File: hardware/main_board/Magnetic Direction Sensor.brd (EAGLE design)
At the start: 49.9 x 49.6 mm, 8 parts, among them J1 5520425-3, J2 5520425-3

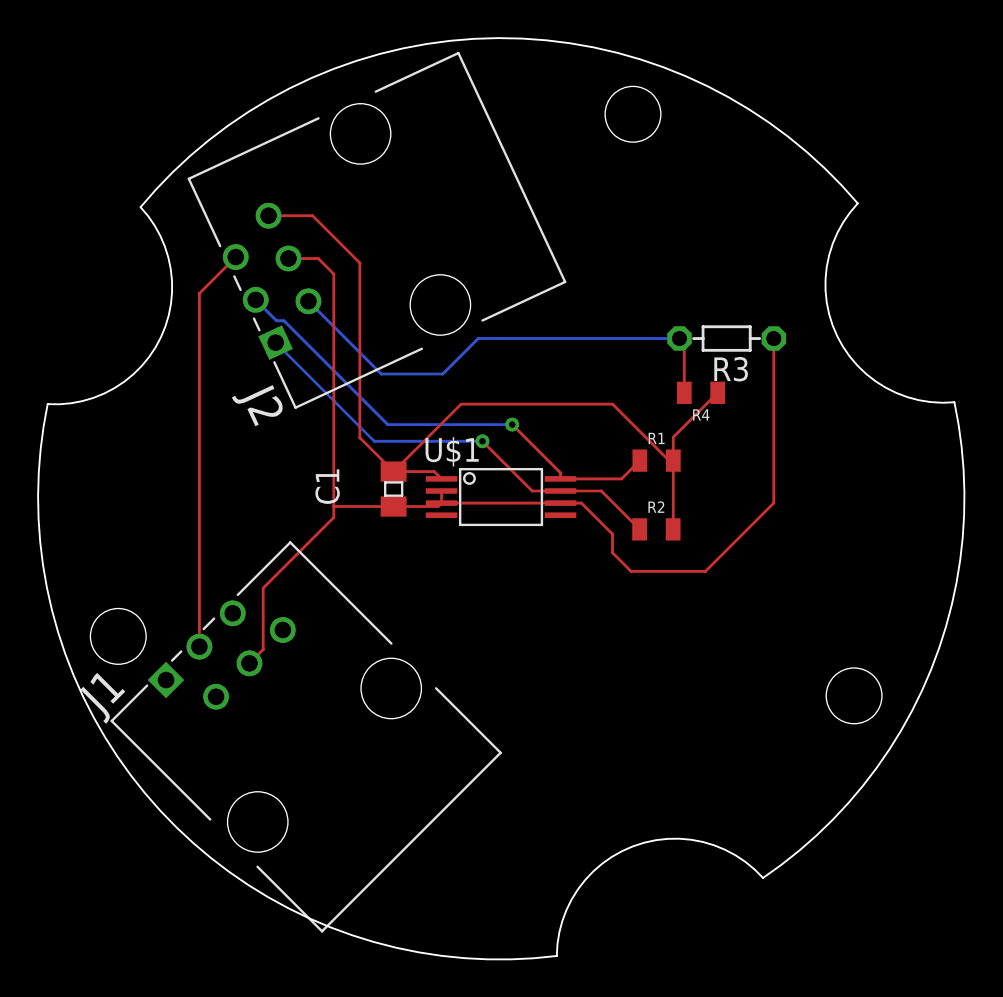
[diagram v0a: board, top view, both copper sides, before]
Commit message: Hardware work. Added elevation to station meta data
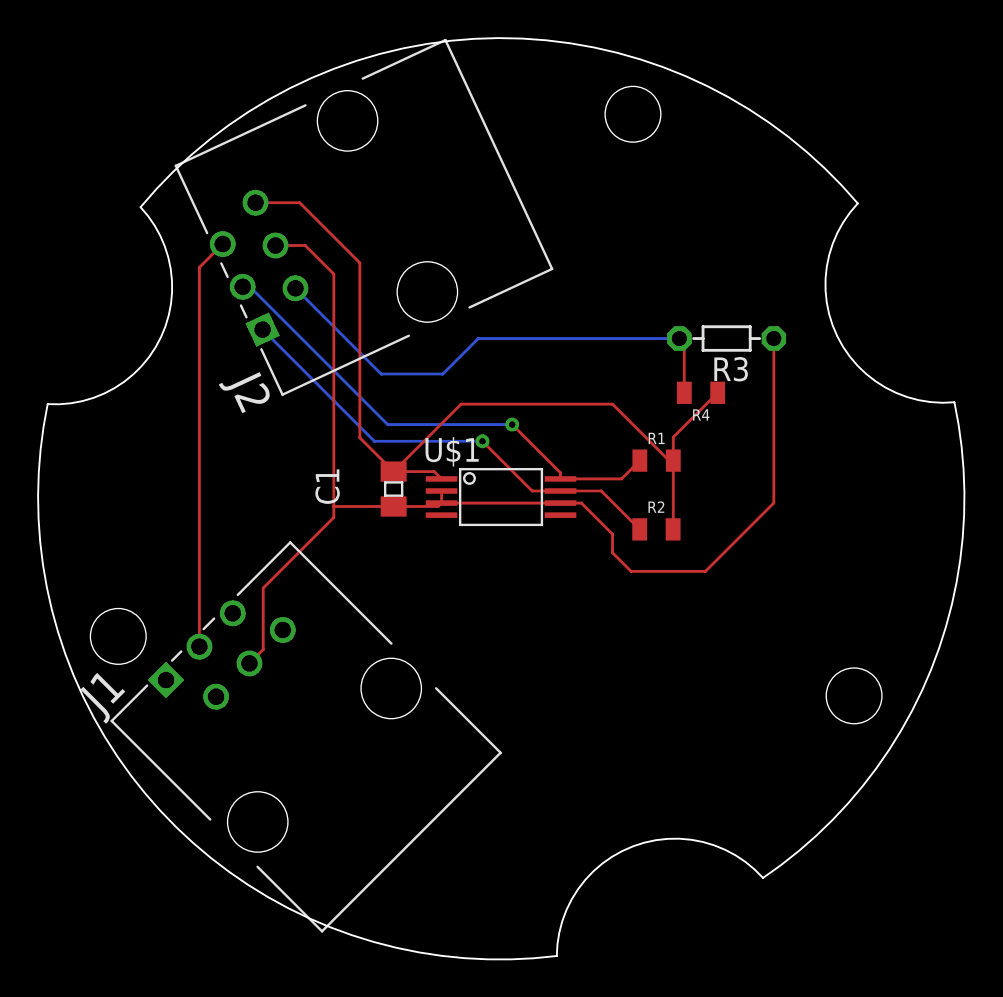
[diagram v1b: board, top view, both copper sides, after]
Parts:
- moved J2 0.99 mm to (12.2, 34.0)
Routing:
- net TS2: track 25.4 -> 26.4 mm
- net SCL: track 25.3 -> 26.3 mm
- net VCC: track 46.8 -> 47.8 mm
- net GND: track 62.5 -> 63.5 mm
- net SDA: track 23.8 -> 24.7 mm
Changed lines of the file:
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@@
 <attribute name="VALUE" x="17.09809375" y="-0.045665625" size="1.77965" layer="27" rot="R45"/>
 </element>
-<element name="J2" library="main_board" package="TE_5520425-3" value="5520425-3" x="12.87" y="33.31" smashed="yes" rot="R115">
-<attribute name="CENTERLINE_PITCH" value="1.02 mm[.04 in]" x="40.655575" y="72.89113125" size="1.778" layer="27" rot="R115" display="off"/>
-<attribute name="COMMENT" value="5520425-3" x="40.655575" y="72.89113125" size="1.778" layer="27" rot="R115" display="off"/>
-<attribute name="DESCRIPTION" value=" Conn RJ-25 F 6 POS 2.54mm Solder ST Thru-Hole 6 Terminal 1 Port Cat 3 Box/Package/Tray " x="40.655575" y="72.89113125" size="1.778" layer="27" rot="R115" display="off"/>
-<attribute name="DIGI-KEY_PART_NUMBER" value="A31415-ND" x="40.655575" y="72.89113125" size="1.778" layer="27" rot="R115" display="off"/>
-<attribute name="DIGI-KEY_PURCHASE_URL" value="https://www.digikey.com/product-detail/en/te-connectivity-amp-connectors/5520425-3/A31415-ND/769559?utm_source=snapeda&amp;utm_medium=aggregator&amp;utm_campaign=symbol" x="40.655575" y="72.89113125" size="1.778" layer="27" rot="R115" display="off"/>
-<attribute name="EU_ROHS_COMPLIANCE" value="Compliant" x="40.655575" y="72.89113125" size="1.778" layer="27" rot="R115" display="off"/>
-<attribute name="MF" value="TE Connectivity" x="40.655575" y="72.89113125" size="1.778" layer="27" rot="R115" display="off"/>
-<attribute name="MP" value="5520425-3" x="40.655575" y="72.89113125" size="1.778" layer="27" rot="R115" display="off"/>
-<attribute name="NAME" x="13.48356875" y="29.363684375" size="1.78073125" layer="25" rot="R115"/>
-<attribute name="NUMBER_OF_POSITIONS" value="6" x="40.655575" y="72.89113125" size="1.778" layer="27" rot="R115" display="off"/>
-<attribute name="PACKAGE" value="None" x="40.655575" y="72.89113125" size="1.778" layer="27" rot="R115" display="off"/>
-<attribute name="TE_PURCHASE_URL" value="https://www.te.com/usa-en/product-5520425-3.html?te_bu=Cor&amp;te_type=disp&amp;te_campaign=seda_glo_cor-seda-global-disp-prtnr-fy19-seda-model-bom-cta_sma-317_1&amp;elqCampaignId=32493" x="40.655575" y="72.89113125" size="1.778" layer="27" rot="R115" display="off"/>
-<attribute name="VALUE" x="30.6132625" y="37.630059375" size="1.77965" layer="27" rot="R115"/>
+<element name="J2" library="main_board" package="TE_5520425-3" value="5520425-3" x="12.17" y="34.01" smashed="yes" rot="R115">
+<attribute name="CENTERLINE_PITCH" value="1.02 mm[.04 in]" x="39.955575" y="73.59113125" size="1.778" layer="27" rot="R115" display="off"/>
+<attribute name="COMMENT" value="5520425-3" x="39.955575" y="73.59113125" size="1.778" layer="27" rot="R115" display="off"/>
+<attribute name="DESCRIPTION" value=" Conn RJ-25 F 6 POS 2.54mm Solder ST Thru-Hole 6 Terminal 1 Port Cat 3 Box/Package/Tray " x="39.955575" y="73.59113125" size="1.778" layer="27" rot="R115" display="off"/>
+<attribute name="DIGI-KEY_PART_NUMBER" value="A31415-ND" x="39.955575" y="73.59113125" size="1.778" layer="27" rot="R115" display="off"/>
+<attribute name="DIGI-KEY_PURCHASE_URL" value="https://www.digikey.com/product-detail/en/te-connectivity-amp-connectors/5520425-3/A31415-ND/769559?utm_source=snapeda&amp;utm_medium=aggregator&amp;utm_campaign=symbol" x="39.955575" y="73.59113125" size="1.778" layer="27" rot="R115" display="off"/>
+<attribute name="EU_ROHS_COMPLIANCE" value="Compliant" x="39.955575" y="73.59113125" size="1.778" layer="27" rot="R115" display="off"/>
+<attribute name="MF" value="TE Connectivity" x="39.955575" y="73.59113125" size="1.778" layer="27" rot="R115" display="off"/>
+<attribute name="MP" value="5520425-3" x="39.955575" y="73.59113125" size="1.778" layer="27" rot="R115" display="off"/>
+<attribute name="NAME" x="12.78356875" y="30.063684375" size="1.78073125" layer="25" rot="R115"/>
+<attribute name="NUMBER_OF_POSITIONS" value="6" x="39.955575" y="73.59113125" size="1.778" layer="27" rot="R115" display="off"/>
+<attribute name="PACKAGE" value="None" x="39.955575" y="73.59113125" size="1.778" layer="27" rot="R115" display="off"/>
+<attribute name="TE_PURCHASE_URL" value="https://www.te.com/usa-en/product-5520425-3.html?te_bu=Cor&amp;te_type=disp&amp;te_campaign=seda_glo_cor-seda-global-disp-prtnr-fy19-seda-model-bom-cta_sma-317_1&amp;elqCampaignId=32493" x="39.955575" y="73.59113125" size="1.778" layer="27" rot="R115" display="off"/>
+<attribute name="VALUE" x="29.9132625" y="38.330059375" size="1.77965" layer="27" rot="R115"/>
 </element>
 <element name="R1" library="SparkFun-Resistors" library_urn="urn:adsk.eagle:library:532" package="0805" package3d_urn="urn:adsk.eagle:package:39651/1" value="2k" x="33.37" y="26.96" smashed="yes">
@@
 <wire x1="19.22" y1="26.3698" x2="17.4" y2="28.1898" width="0.1524" layer="1"/>
 <wire x1="17.4" y1="28.1898" x2="17.4" y2="37.6" width="0.1524" layer="1"/>
-<wire x1="17.4" y1="37.6" x2="14.861496875" y2="40.138503125" width="0.1524" layer="1"/>
-<wire x1="14.861496875" y1="40.138503125" x2="12.48839375" y2="40.138503125" width="0.1524" layer="1"/>
+<wire x1="17.4" y1="37.6" x2="14.161496875" y2="40.838503125" width="0.1524" layer="1"/>
+<wire x1="14.161496875" y1="40.838503125" x2="11.78839375" y2="40.838503125" width="0.1524" layer="1"/>
 <wire x1="34.27" y1="26.96" x2="34.04" y2="26.96" width="0.1524" layer="1"/>
 <wire x1="34.04" y1="26.96" x2="31" y2="30" width="0.1524" layer="1"/>
@@
 <wire x1="19.22" y1="24.4902" x2="21.6152" y2="24.4902" width="0.1524" layer="1"/>
 <wire x1="21.6152" y1="24.4902" x2="21.8" y2="24.675" width="0.1524" layer="1"/>
-<wire x1="13.56184375" y1="37.83648125" x2="15.16351875" y2="37.83648125" width="0.1524" layer="1"/>
-<wire x1="15.16351875" y1="37.83648125" x2="16" y2="37" width="0.1524" layer="1"/>
+<wire x1="12.86184375" y1="38.53648125" x2="14.46351875" y2="38.53648125" width="0.1524" layer="1"/>
+<wire x1="14.46351875" y1="38.53648125" x2="16" y2="37" width="0.1524" layer="1"/>
 <wire x1="16" y1="37" x2="16" y2="24.5" width="0.1524" layer="1"/>
 <wire x1="16" y1="24.5" x2="16" y2="23.9" width="0.1524" layer="1"/>
@@
 <wire x1="32.46" y1="23.26" x2="30.395" y2="25.325" width="0.1524" layer="1"/>
 <wire x1="30.395" y1="25.325" x2="28.2" y2="25.325" width="0.1524" layer="1"/>
-<wire x1="12.87" y1="33.31" x2="18.18" y2="28" width="0.1524" layer="16"/>
+<wire x1="12.17" y1="34.01" x2="18.18" y2="28" width="0.1524" layer="16"/>
 <wire x1="18.18" y1="28" x2="24" y2="28" width="0.1524" layer="16"/>
 <via x="24" y="28" extent="1-16" drill="0.35"/>
@@
 <wire x1="31.485" y1="25.975" x2="28.2" y2="25.975" width="0.1524" layer="1"/>
 <via x="25.6" y="28.9" extent="1-16" drill="0.35"/>
-<wire x1="11.796546875" y1="35.61201875" x2="12.922446875" y2="34.48611875" width="0.1524" layer="16"/>
-<wire x1="12.922446875" y1="34.48611875" x2="13.31049375" y2="34.48611875" width="0.1524" layer="16"/>
-<wire x1="18.8966125" y1="28.9" x2="25.6" y2="28.9" width="0.1524" layer="16"/>
-<wire x1="13.31049375" y1="34.48611875" x2="18.8966125" y2="28.9" width="0.1524" layer="16"/>
+<wire x1="25.6" y1="28.9" x2="18.8966125" y2="28.9" width="0.1524" layer="16"/>
 <wire x1="25.6" y1="28.9" x2="28.2" y2="26.3" width="0.1524" layer="1"/>
 <wire x1="28.2" y1="26.3" x2="28.2" y2="25.975" width="0.1524" layer="1"/>
+<wire x1="11.48459375" y1="36.31201875" x2="11.096546875" y2="36.31201875" width="0.1524" layer="16"/>
+<wire x1="18.8966125" y1="28.9" x2="11.48459375" y2="36.31201875" width="0.1524" layer="16"/>
 </signal>
 <signal name="TS2">
@@
 <wire x1="23.77095625" y1="33.53" x2="21.85978125" y2="31.618825" width="0.1524" layer="16"/>
 <wire x1="21.85978125" y1="31.618825" x2="18.550928125" y2="31.618825" width="0.1524" layer="16"/>
-<wire x1="18.550928125" y1="31.618825" x2="14.63529375" y2="35.534459375" width="0.1524" layer="16"/>
+<wire x1="18.550928125" y1="31.618825" x2="13.93529375" y2="36.234459375" width="0.1524" layer="16"/>
 </signal>
 <signal name="WIND_SPD">
 <contactref element="J1" pad="3"/>
 <contactref element="J2" pad="5"/>
-<wire x1="8.76605" y1="16.94605" x2="8.76605" y2="35.95699375" width="0.1524" layer="1"/>
-<wire x1="8.76605" y1="35.95699375" x2="10.723096875" y2="37.914040625" width="0.1524" layer="1"/>
+<wire x1="8.76605" y1="16.94605" x2="8.76605" y2="37.35699375" width="0.1524" layer="1"/>
+<wire x1="8.76605" y1="37.35699375" x2="10.023096875" y2="38.614040625" width="0.1524" layer="1"/>
 </signal>
 </signals>
